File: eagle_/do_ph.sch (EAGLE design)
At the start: 25 parts, among them IC1 MEGA8-P, Q1 8Mhz

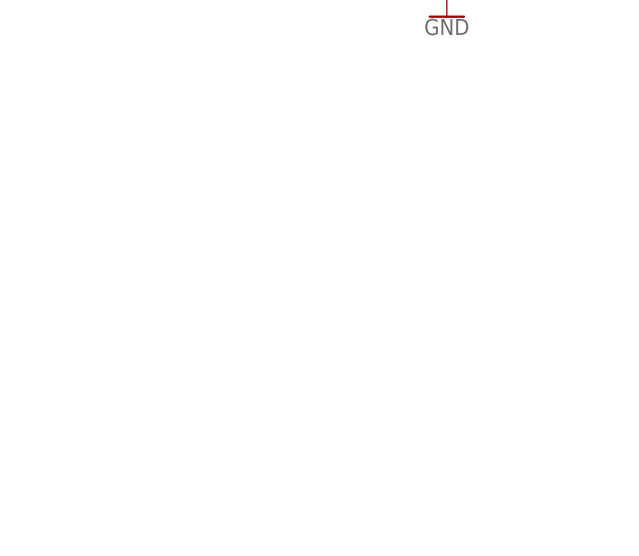
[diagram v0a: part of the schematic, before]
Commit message: thêm jack nap code
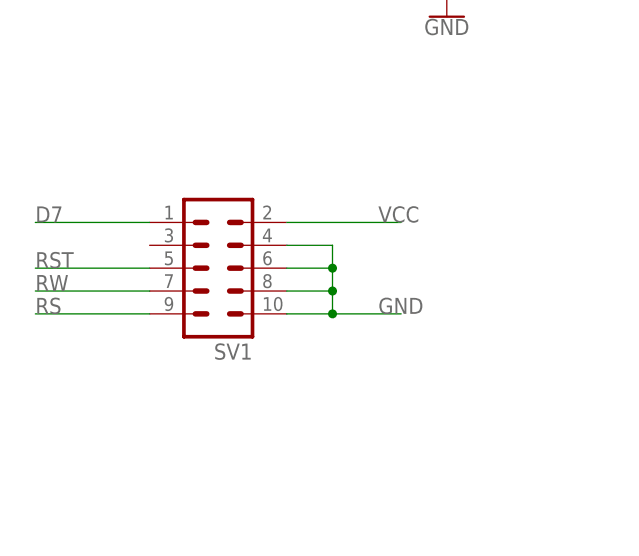
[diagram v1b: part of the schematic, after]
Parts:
- added SV1: (no value), con-lstb:MA05-2
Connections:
- net D7: now also SV1.1
- net GND: now also SV1.10, SV1.4, SV1.6, SV1.8
- net RS: now also SV1.9
- net RST: now also SV1.5
- net RW: now also SV1.7
- net VCC: now also SV1.2
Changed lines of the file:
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@@
 <part name="S3" library="switch-omron" library_urn="urn:adsk.eagle:library:377" deviceset="10-XX" device="" package3d_urn="urn:adsk.eagle:package:27496/1"/>
 <part name="R_S3" library="adafruit" deviceset="R-US_" device="R0805" value="10k"/>
+<part name="SV1" library="con-lstb" library_urn="urn:adsk.eagle:library:162" deviceset="MA05-2" device="" package3d_urn="urn:adsk.eagle:package:8329/1"/>
 </parts>
 <sheets>
@@
 <attribute name="NAME" x="151.3586" y="97.79" size="1.778" layer="95" rot="MR90"/>
 <attribute name="VALUE" x="146.558" y="97.79" size="1.778" layer="96" rot="MR90"/>
+</instance>
+<instance part="SV1" gate="G$1" x="-15.24" y="-7.62" smashed="yes" rot="R180">
+<attribute name="VALUE" x="-11.43" y="2.54" size="1.778" layer="96" rot="R180"/>
+<attribute name="NAME" x="-11.43" y="-16.002" size="1.778" layer="95" rot="R180"/>
 </instance>
 </instances>
@@
 <pinref part="C6" gate="G$1" pin="1"/>
 </segment>
+<segment>
+<pinref part="SV1" gate="G$1" pin="10"/>
+<wire x1="-7.62" y1="-12.7" x2="-2.54" y2="-12.7" width="0.1524" layer="91"/>
+<label x="2.54" y="-12.7" size="1.778" layer="95"/>
+<pinref part="SV1" gate="G$1" pin="4"/>
+<wire x1="-2.54" y1="-12.7" x2="5.08" y2="-12.7" width="0.1524" layer="91"/>
+<wire x1="-7.62" y1="-5.08" x2="-2.54" y2="-5.08" width="0.1524" layer="91"/>
+<wire x1="-2.54" y1="-5.08" x2="-2.54" y2="-7.62" width="0.1524" layer="91"/>
+<junction x="-2.54" y="-12.7"/>
+<pinref part="SV1" gate="G$1" pin="6"/>
+<wire x1="-2.54" y1="-7.62" x2="-2.54" y2="-10.16" width="0.1524" layer="91"/>
+<wire x1="-2.54" y1="-10.16" x2="-2.54" y2="-12.7" width="0.1524" layer="91"/>
+<wire x1="-7.62" y1="-7.62" x2="-2.54" y2="-7.62" width="0.1524" layer="91"/>
+<junction x="-2.54" y="-7.62"/>
+<pinref part="SV1" gate="G$1" pin="8"/>
+<wire x1="-7.62" y1="-10.16" x2="-2.54" y2="-10.16" width="0.1524" layer="91"/>
+<junction x="-2.54" y="-10.16"/>
+</segment>
 </net>
 <net name="VCC" class="0">
@@
 <pinref part="U$5" gate="G$1" pin="P_VCC"/>
 </segment>
+<segment>
+<pinref part="SV1" gate="G$1" pin="2"/>
+<wire x1="-7.62" y1="-2.54" x2="5.08" y2="-2.54" width="0.1524" layer="91"/>
+<label x="2.54" y="-2.54" size="1.778" layer="95"/>
+</segment>
 </net>
 <net name="D4" class="0">
@@
 <label x="170.922" y="-17.642" size="1.778" layer="95"/>
 </segment>
+<segment>
+<pinref part="SV1" gate="G$1" pin="1"/>
+<wire x1="-22.86" y1="-2.54" x2="-35.56" y2="-2.54" width="0.1524" layer="91"/>
+<label x="-35.56" y="-2.54" size="1.778" layer="95"/>
+</segment>
 </net>
 <net name="RS" class="0">
@@
 <label x="173.482" y="-18.542" size="1.778" layer="95" rot="R180"/>
 </segment>
+<segment>
+<pinref part="SV1" gate="G$1" pin="9"/>
+<wire x1="-22.86" y1="-12.7" x2="-35.56" y2="-12.7" width="0.1524" layer="91"/>
+<label x="-35.56" y="-12.7" size="1.778" layer="95"/>
+</segment>
 </net>
 <net name="RW" class="0">
@@
 <wire x1="163.068" y1="-22.86" x2="173.482" y2="-22.86" width="0.1524" layer="91"/>
 <label x="173.482" y="-21.082" size="1.778" layer="95" rot="R180"/>
+</segment>
+<segment>
+<pinref part="SV1" gate="G$1" pin="7"/>
+<wire x1="-22.86" y1="-10.16" x2="-35.56" y2="-10.16" width="0.1524" layer="91"/>
+<label x="-35.56" y="-10.16" size="1.778" layer="95"/>
 </segment>
 </net>
@@
 <label x="162.56" y="60.96" size="1.778" layer="95"/>
 </segment>
-</net>
+<segment>
+<pinref part="SV1" gate="G$1" pin="5"/>
+<wire x1="-22.86" y1="-7.62" x2="-35.56" y2="-7.62" width="0.1524" layer="91"/>
+<label x="-35.56" y="-7.62" size="1.778" layer="95"/>
+</segment>
+</net>

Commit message: update
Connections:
- new net RX: IC1.PD0(RXD), SV1.4
- new net TX: IC1.PD1(TXD), SV1.6
- net GND: no longer SV1.4, SV1.6
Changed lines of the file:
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@@
 <segment>
 <pinref part="SV1" gate="G$1" pin="10"/>
-<wire x1="-7.62" y1="-12.7" x2="-2.54" y2="-12.7" width="0.1524" layer="91"/>
 <label x="2.54" y="-12.7" size="1.778" layer="95"/>
-<pinref part="SV1" gate="G$1" pin="4"/>
-<wire x1="-2.54" y1="-12.7" x2="5.08" y2="-12.7" width="0.1524" layer="91"/>
-<wire x1="-7.62" y1="-5.08" x2="-2.54" y2="-5.08" width="0.1524" layer="91"/>
-<wire x1="-2.54" y1="-5.08" x2="-2.54" y2="-7.62" width="0.1524" layer="91"/>
-<junction x="-2.54" y="-12.7"/>
-<pinref part="SV1" gate="G$1" pin="6"/>
-<wire x1="-2.54" y1="-7.62" x2="-2.54" y2="-10.16" width="0.1524" layer="91"/>
-<wire x1="-2.54" y1="-10.16" x2="-2.54" y2="-12.7" width="0.1524" layer="91"/>
-<wire x1="-7.62" y1="-7.62" x2="-2.54" y2="-7.62" width="0.1524" layer="91"/>
-<junction x="-2.54" y="-7.62"/>
+<wire x1="-7.62" y1="-12.7" x2="-5.08" y2="-12.7" width="0.1524" layer="91"/>
 <pinref part="SV1" gate="G$1" pin="8"/>
-<wire x1="-7.62" y1="-10.16" x2="-2.54" y2="-10.16" width="0.1524" layer="91"/>
-<junction x="-2.54" y="-10.16"/>
+<wire x1="-5.08" y1="-12.7" x2="5.08" y2="-12.7" width="0.1524" layer="91"/>
+<wire x1="-7.62" y1="-10.16" x2="-5.08" y2="-10.16" width="0.1524" layer="91"/>
+<wire x1="-5.08" y1="-10.16" x2="-5.08" y2="-12.7" width="0.1524" layer="91"/>
+<junction x="-5.08" y="-12.7"/>
 </segment>
 </net>
@@
 </segment>
 </net>
+<net name="RX" class="0">
+<segment>
+<pinref part="IC1" gate="G$1" pin="PD0(RXD)"/>
+<wire x1="163.068" y1="12.7" x2="175.26" y2="12.7" width="0.1524" layer="91"/>
+<label x="172.72" y="12.7" size="1.778" layer="95"/>
+</segment>
+<segment>
+<pinref part="SV1" gate="G$1" pin="4"/>
+<wire x1="-7.62" y1="-5.08" x2="5.08" y2="-5.08" width="0.1524" layer="91"/>
+<label x="2.54" y="-5.08" size="1.778" layer="95"/>
+</segment>
+</net>
+<net name="TX" class="0">
+<segment>
+<pinref part="IC1" gate="G$1" pin="PD1(TXD)"/>
+<wire x1="163.068" y1="10.16" x2="175.26" y2="10.16" width="0.1524" layer="91"/>
+<label x="172.72" y="10.16" size="1.778" layer="95"/>
+</segment>
+<segment>
+<pinref part="SV1" gate="G$1" pin="6"/>
+<wire x1="-7.62" y1="-7.62" x2="5.08" y2="-7.62" width="0.1524" layer="91"/>
+<label x="2.54" y="-7.62" size="1.778" layer="95"/>
+</segment>
+</net>

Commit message: update
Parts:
- removed SV1: (no value), con-lstb:MA05-2
- removed U$6: RM065_V1, RM065:RM065_V1
- added SV2: (no value), con-lsta:FE07-2
- added U$2: RES_RM063, res_RM063:RES_RM063
- renumbered S3 to RST
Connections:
- net D7: now also SV2.6; no longer SV1.1
- net GND: now also SV2.11, SV2.13, SV2.7, SV2.9, U$2.P$2; no longer SV1.10, SV1.8, U$6.P$2
- net N$1: now also U$2.P$3; no longer U$6.P$3
- net RS: now also SV2.14; no longer SV1.9
- net RST: now also SV2.10; no longer SV1.5
- net RW: now also SV2.12; no longer SV1.7
- net RX: now also SV2.1; no longer SV1.4
- net TX: now also SV2.3; no longer SV1.6
- net VCC: now also SV2.5, U$2.P$1; no longer SV1.2, U$6.P$1
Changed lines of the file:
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@@
 <?xml version="1.0" encoding="utf-8"?>
 <!DOCTYPE eagle SYSTEM "eagle.dtd">
-<eagle version="9.3.1">
+<eagle version="9.3.2">
 <drawing>
 <settings>
@@
 <part name="C6" library="SparkFun-Capacitors" deviceset="1.0UF" device="-0805-25V-(+80/-20%)" value="22pF"/>
 <part name="U$5" library="PH_SENSOR_DFROBOT" deviceset="PH_SENSOR_DFROBOT" device=""/>
-<part name="U$6" library="RM065" deviceset="RM065_V1" device=""/>
-<part name="S3" library="switch-omron" library_urn="urn:adsk.eagle:library:377" deviceset="10-XX" device="" package3d_urn="urn:adsk.eagle:package:27496/1"/>
+<part name="RST" library="switch-omron" library_urn="urn:adsk.eagle:library:377" deviceset="10-XX" device="" package3d_urn="urn:adsk.eagle:package:27496/1"/>
 <part name="R_S3" library="adafruit" deviceset="R-US_" device="R0805" value="10k"/>
-<part name="SV1" library="con-lstb" library_urn="urn:adsk.eagle:library:162" deviceset="MA05-2" device="" package3d_urn="urn:adsk.eagle:package:8329/1"/>
+<part name="U$2" library="res_RM063" deviceset="RES_RM063" device=""/>
+<part name="SV2" library="con-lsta" library_urn="urn:adsk.eagle:library:161" deviceset="FE07-2" device="" package3d_urn="urn:adsk.eagle:package:8182/1"/>
 </parts>
 <sheets>
@@
 </instance>
 <instance part="U$5" gate="G$1" x="165.1" y="45.72" smashed="yes"/>
-<instance part="U$6" gate="G$1" x="-30.48" y="91.44" smashed="yes" rot="R270">
-<attribute name="NAME" x="-36.6014" y="95.25" size="1.778" layer="95" rot="R270"/>
-<attribute name="VALUE" x="-33.782" y="95.25" size="1.778" layer="96" rot="R270"/>
-</instance>
-<instance part="S3" gate="1" x="116.84" y="63.5" smashed="yes" rot="R270">
+<instance part="RST" gate="1" x="116.84" y="63.5" smashed="yes" rot="R270">
 <attribute name="NAME" x="114.3" y="69.85" size="1.778" layer="95"/>
 <attribute name="VALUE" x="120.015" y="67.31" size="1.778" layer="96"/>
@@
 <attribute name="VALUE" x="146.558" y="97.79" size="1.778" layer="96" rot="MR90"/>
 </instance>
-<instance part="SV1" gate="G$1" x="-15.24" y="-7.62" smashed="yes" rot="R180">
-<attribute name="VALUE" x="-11.43" y="2.54" size="1.778" layer="96" rot="R180"/>
-<attribute name="NAME" x="-11.43" y="-16.002" size="1.778" layer="95" rot="R180"/>
+<instance part="U$2" gate="G$1" x="-30.48" y="91.44" smashed="yes" rot="R270">
+<attribute name="NAME" x="-36.6014" y="95.25" size="1.778" layer="95" rot="R270"/>
+<attribute name="VALUE" x="-33.782" y="95.25" size="1.778" layer="96" rot="R270"/>
+</instance>
+<instance part="SV2" gate="G$1" x="-68.58" y="2.54" smashed="yes" rot="R180">
+<attribute name="VALUE" x="-64.77" y="15.24" size="1.778" layer="96" rot="R180"/>
+<attribute name="NAME" x="-64.77" y="-8.382" size="1.778" layer="95" rot="R180"/>
 </instance>
 </instances>
@@
 <wire x1="27.94" y1="83.82" x2="7.62" y2="83.82" width="0.1524" layer="91"/>
 <junction x="7.62" y="83.82"/>
-<pinref part="U$6" gate="G$1" pin="P$2"/>
+<pinref part="U$2" gate="G$1" pin="P$2"/>
 </segment>
 <segment>
@@
 <junction x="104.14" y="73.66"/>
 <label x="93.98" y="73.66" size="1.778" layer="95"/>
-<pinref part="S3" gate="1" pin="P1"/>
+<pinref part="RST" gate="1" pin="P1"/>
 <wire x1="111.76" y1="60.96" x2="104.14" y2="60.96" width="0.1524" layer="91"/>
 <wire x1="104.14" y1="60.96" x2="104.14" y2="63.5" width="0.1524" layer="91"/>
-<pinref part="S3" gate="1" pin="P"/>
+<pinref part="RST" gate="1" pin="P"/>
 <wire x1="104.14" y1="63.5" x2="104.14" y2="73.66" width="0.1524" layer="91"/>
 <wire x1="111.76" y1="63.5" x2="104.14" y2="63.5" width="0.1524" layer="91"/>
@@
 </segment>
 <segment>
-<pinref part="SV1" gate="G$1" pin="10"/>
-<label x="2.54" y="-12.7" size="1.778" layer="95"/>
-<wire x1="-7.62" y1="-12.7" x2="-5.08" y2="-12.7" width="0.1524" layer="91"/>
-<pinref part="SV1" gate="G$1" pin="8"/>
-<wire x1="-5.08" y1="-12.7" x2="5.08" y2="-12.7" width="0.1524" layer="91"/>
-<wire x1="-7.62" y1="-10.16" x2="-5.08" y2="-10.16" width="0.1524" layer="91"/>
-<wire x1="-5.08" y1="-10.16" x2="-5.08" y2="-12.7" width="0.1524" layer="91"/>
-<junction x="-5.08" y="-12.7"/>
+<pinref part="SV2" gate="G$1" pin="13"/>
+<wire x1="-60.96" y1="-5.08" x2="-55.88" y2="-5.08" width="0.1524" layer="91"/>
+<label x="-50.8" y="-5.08" size="1.778" layer="95" rot="MR0"/>
+<pinref part="SV2" gate="G$1" pin="7"/>
+<wire x1="-55.88" y1="-5.08" x2="-50.8" y2="-5.08" width="0.1524" layer="91"/>
+<wire x1="-60.96" y1="2.54" x2="-55.88" y2="2.54" width="0.1524" layer="91"/>
+<wire x1="-55.88" y1="2.54" x2="-55.88" y2="0" width="0.1524" layer="91"/>
+<junction x="-55.88" y="-5.08"/>
+<pinref part="SV2" gate="G$1" pin="9"/>
+<wire x1="-55.88" y1="0" x2="-55.88" y2="-2.54" width="0.1524" layer="91"/>
+<wire x1="-55.88" y1="-2.54" x2="-55.88" y2="-5.08" width="0.1524" layer="91"/>
+<wire x1="-60.96" y1="0" x2="-55.88" y2="0" width="0.1524" layer="91"/>
+<junction x="-55.88" y="0"/>
+<pinref part="SV2" gate="G$1" pin="11"/>
+<wire x1="-60.96" y1="-2.54" x2="-55.88" y2="-2.54" width="0.1524" layer="91"/>
+<junction x="-55.88" y="-2.54"/>
 </segment>
 </net>
@@
 <wire x1="-25.4" y1="101.6" x2="-30.48" y2="101.6" width="0.1524" layer="91"/>
 <junction x="-30.48" y="101.6"/>
-<pinref part="U$6" gate="G$1" pin="P$1"/>
+<pinref part="U$2" gate="G$1" pin="P$1"/>
 </segment>
 <segment>
@@
 </segment>
 <segment>
-<pinref part="SV1" gate="G$1" pin="2"/>
-<wire x1="-7.62" y1="-2.54" x2="5.08" y2="-2.54" width="0.1524" layer="91"/>
-<label x="2.54" y="-2.54" size="1.778" layer="95"/>
+<pinref part="SV2" gate="G$1" pin="5"/>
+<wire x1="-60.96" y1="5.08" x2="-50.8" y2="5.08" width="0.1524" layer="91"/>
+<label x="-50.8" y="5.08" size="1.778" layer="95" rot="MR0"/>
 </segment>
 </net>
@@
 </segment>
 <segment>
-<pinref part="SV1" gate="G$1" pin="1"/>
-<wire x1="-22.86" y1="-2.54" x2="-35.56" y2="-2.54" width="0.1524" layer="91"/>
-<label x="-35.56" y="-2.54" size="1.778" layer="95"/>
+<pinref part="SV2" gate="G$1" pin="6"/>
+<wire x1="-76.2" y1="5.08" x2="-88.9" y2="5.08" width="0.1524" layer="91"/>
+<label x="-83.82" y="5.08" size="1.778" layer="95" rot="MR0"/>
 </segment>
 </net>
@@
 </segment>
 <segment>
-<pinref part="SV1" gate="G$1" pin="9"/>
-<wire x1="-22.86" y1="-12.7" x2="-35.56" y2="-12.7" width="0.1524" layer="91"/>
-<label x="-35.56" y="-12.7" size="1.778" layer="95"/>
+<pinref part="SV2" gate="G$1" pin="14"/>
+<wire x1="-76.2" y1="-5.08" x2="-88.9" y2="-5.08" width="0.1524" layer="91"/>
+<label x="-83.82" y="-5.08" size="1.778" layer="95" rot="MR0"/>
 </segment>
 </net>
@@
 </segment>
 <segment>
-<pinref part="SV1" gate="G$1" pin="7"/>
-<wire x1="-22.86" y1="-10.16" x2="-35.56" y2="-10.16" width="0.1524" layer="91"/>
-<label x="-35.56" y="-10.16" size="1.778" layer="95"/>
+<pinref part="SV2" gate="G$1" pin="12"/>
+<wire x1="-76.2" y1="-2.54" x2="-88.9" y2="-2.54" width="0.1524" layer="91"/>
+<label x="-83.82" y="-2.54" size="1.778" layer="95" rot="MR0"/>
 </segment>
 </net>
@@
 <wire x1="-5.08" y1="91.44" x2="-5.08" y2="104.14" width="0.1524" layer="91"/>
 <wire x1="-25.4" y1="91.44" x2="-5.08" y2="91.44" width="0.1524" layer="91"/>
-<pinref part="U$6" gate="G$1" pin="P$3"/>
+<pinref part="U$2" gate="G$1" pin="P$3"/>
 </segment>
 </net>
@@
 </segment>
 <segment>
-<pinref part="S3" gate="1" pin="S1"/>
+<pinref part="RST" gate="1" pin="S1"/>
 <pinref part="R_S3" gate="G$1" pin="1"/>
 <wire x1="121.92" y1="60.96" x2="124.46" y2="60.96" width="0.1524" layer="91"/>
 <wire x1="124.46" y1="60.96" x2="149.86" y2="60.96" width="0.1524" layer="91"/>
 <wire x1="149.86" y1="60.96" x2="149.86" y2="96.52" width="0.1524" layer="91"/>
-<pinref part="S3" gate="1" pin="S"/>
+<pinref part="RST" gate="1" pin="S"/>
 <wire x1="121.92" y1="63.5" x2="124.46" y2="63.5" width="0.1524" layer="91"/>
 <wire x1="124.46" y1="63.5" x2="124.46" y2="60.96" width="0.1524" layer="91"/>
@@
 </segment>
 <segment>
-<pinref part="SV1" gate="G$1" pin="5"/>
-<wire x1="-22.86" y1="-7.62" x2="-35.56" y2="-7.62" width="0.1524" layer="91"/>
-<label x="-35.56" y="-7.62" size="1.778" layer="95"/>
+<pinref part="SV2" gate="G$1" pin="10"/>
+<wire x1="-76.2" y1="0" x2="-88.9" y2="0" width="0.1524" layer="91"/>
+<label x="-83.82" y="0" size="1.778" layer="95" rot="MR0"/>
 </segment>
 </net>
@@
 </segment>
 <segment>
-<pinref part="SV1" gate="G$1" pin="4"/>
-<wire x1="-7.62" y1="-5.08" x2="5.08" y2="-5.08" width="0.1524" layer="91"/>
-<label x="2.54" y="-5.08" size="1.778" layer="95"/>
+<pinref part="SV2" gate="G$1" pin="1"/>
+<wire x1="-60.96" y1="10.16" x2="-50.8" y2="10.16" width="0.1524" layer="91"/>
+<label x="-55.88" y="10.16" size="1.778" layer="95"/>
 </segment>
 </net>
@@
 </segment>
 <segment>
-<pinref part="SV1" gate="G$1" pin="6"/>
-<wire x1="-7.62" y1="-7.62" x2="5.08" y2="-7.62" width="0.1524" layer="91"/>
-<label x="2.54" y="-7.62" size="1.778" layer="95"/>
-</segment>
-</net>
+<pinref part="SV2" gate="G$1" pin="3"/>
+<wire x1="-60.96" y1="7.62" x2="-50.8" y2="7.62" width="0.1524" layer="91"/>
+<label x="-55.88" y="7.62" size="1.778" layer="95"/>
+</segment>
+</net>

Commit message: update
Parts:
- removed C5, C6: 22pF, SparkFun-Capacitors:1.0UF-0805-25V-(+80/-20%)
- added C1, C2: 22pF, SparkFun-Retired:2.2UF-CERCAP-07888
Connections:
- net GND: now also C1.1, C2.1; no longer C5.1, C6.1
- net XTA1: now also C1.2; no longer C5.2
- net XTA2: now also C2.2; no longer C6.2
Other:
- moved on the sheet: C4, C_N1, C_N2, C_N3, C_N4, IC1, L, LED1, Q1, R, R1, RST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
